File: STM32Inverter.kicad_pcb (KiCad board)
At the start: 4 copper layers, 100 x 100 mm, 151 parts, among them J1 STLINK, J2 CURRENT SENSE, J5 UART, J6 INTERFACE, J7 POWER, J8 501571-2007, J9 RESOLVER, Q1 BCX54, Q2 BCX55, Q4 ST3422A, Q5 BCX54, Q6 BCX55, U1 STM32F303VCTx, U10 ULN2002, U11 LM393, U12 LM393, U2 LM358, U3 AD2S1205, U4 74HCT00, U5 74HCT04, U6 74HCT08, U7 MCP2551-I-SN, U8 74HCT08, U9 74HCT08, Y2 CSTNE8M00GH5C000R0, Y3 CSTNE8M00GH5C000R0

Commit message: Board enven more done
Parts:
- moved C14 1.07 mm to (68.2, 72.8)
- moved C16 0.88 mm to (64.3, 72.8)
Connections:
- U1 pad 73: unconnected-(U1-PF6-Pad73) -> /LED_PIN
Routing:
- net /LED_PIN: track 0.00 -> 18.0 mm, vias 0 -> 2
- net GND: track 81.7 -> 95.6 mm, vias 48 -> 60
- net +5V: track 198.0 -> 211.9 mm, vias 10 -> 11
- net /FAULT_DRV: track 97.2 -> 92.1 mm
- net /VBUS_DRV: track 85.0 -> 81.3 mm
- net /PWM_CH1N: track 78.1 -> 74.4 mm
- net /COS_L: track 52.4 -> 55.5 mm
- net /AD2S1205/Vcc/2: track 15.6 -> 18.5 mm, vias 0 -> 2
- net /ACC_INPUT_A_3V3: track 21.7 -> 24.2 mm
- net /COS_H: track 57.1 -> 59.3 mm
- net Net-(D5-A): track 0.00 -> 2.15 mm
- net Net-(U3-REFBYP): track 2.52 -> 3.29 mm
- net +15V: track 214.7 -> 215.3 mm
- net +5VA: track 127.5 -> 126.9 mm
- net Net-(D2-K): vias 1 -> 2
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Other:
- board text added: "STM32INVERTER MITSUBISHI REMCU Jelcz Industries knowak.xyz"

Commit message: Awaiting review
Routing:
- net +3V3: track 126.2 -> 143.1 mm, vias 17 -> 18
- net +5V: track 211.9 -> 209.0 mm
- net GND: track 95.6 -> 97.6 mm
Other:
- board text added: "1"
- board text added: "DRIVER BOARD"
- board text added: "HALL"
- board text added: "I/O"
- board text added: "MOTOR"
- board text added: "Michał Zychla Krzysztof Nowak"
- board text added: "POWER"
- board text added: "STM32INVERTER MITSUBISHI REMCU Jelcz Industries knowak.xyz 2023"
- board text added: "SWD"
- board text added: "UART"
- board text removed: "STM32INVERTER MITSUBISHI REMCU Jelcz Industries knowak.xyz"

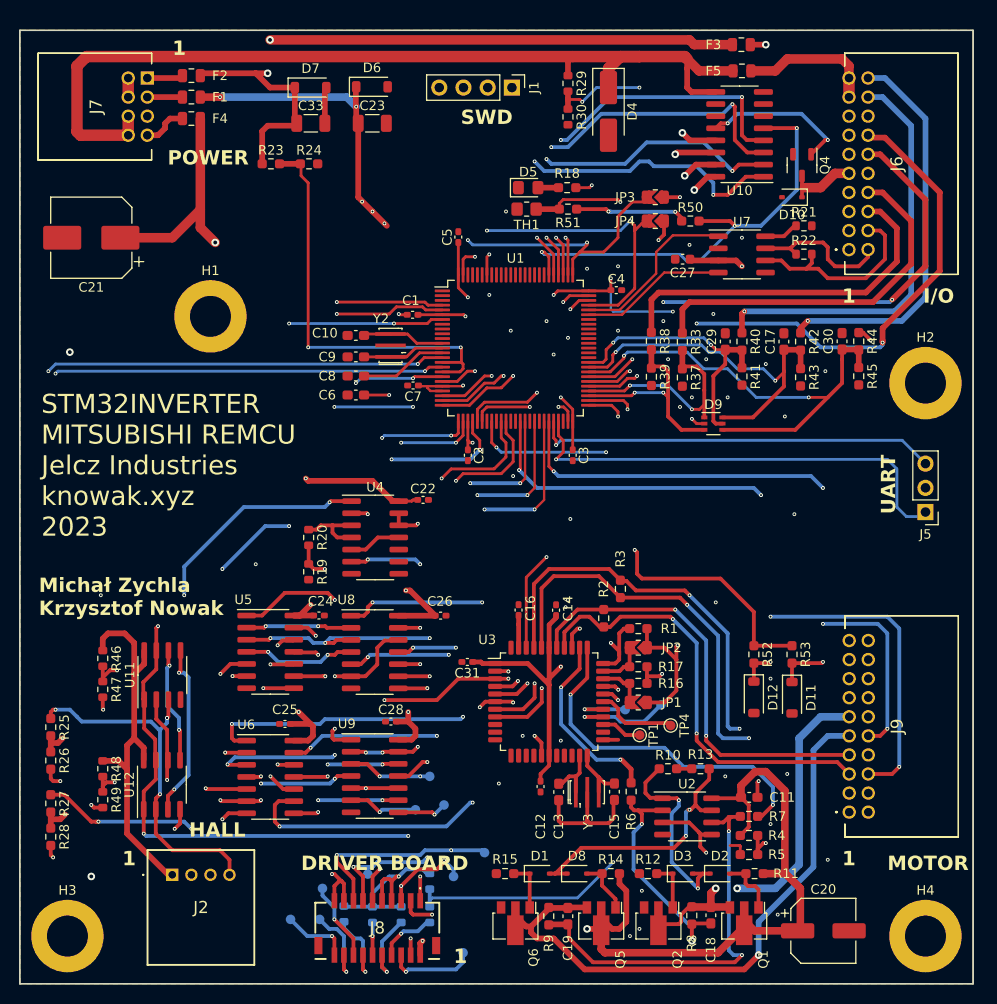
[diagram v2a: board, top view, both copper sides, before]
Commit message: Fix DRC warnings and exclude jumper errors
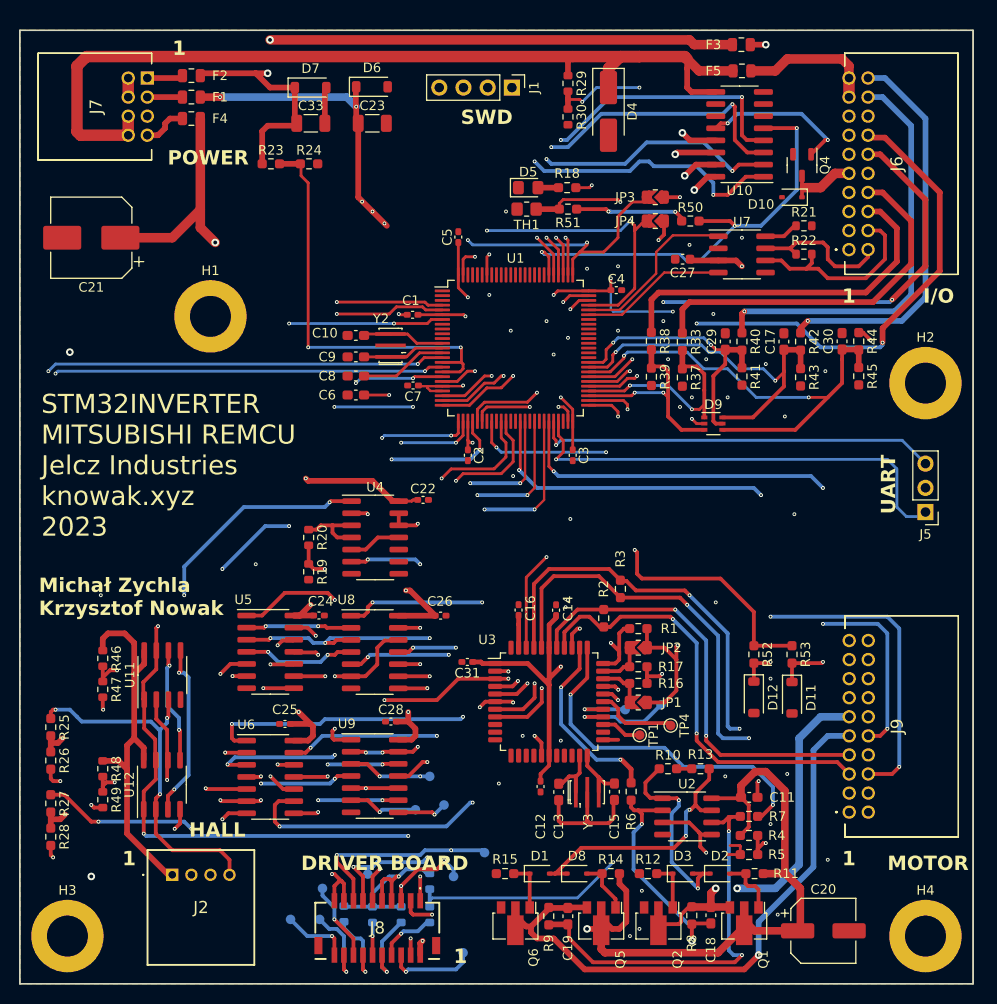
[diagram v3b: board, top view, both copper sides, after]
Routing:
- net GND: track 97.6 -> 99.0 mm
- net /AUX_IN: track 50.3 -> 49.8 mm
- net /CURRENT_B_RAW: vias 4 -> 3
- net /CS_RES: vias 5 -> 4
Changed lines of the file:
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@@
     (property "ki_keywords" "diode")
     (attr smd)
-    (fp_text reference "D10" (at 0 -1.85) (layer "F.SilkS")
+    (fp_text reference "D10" (at 3.25 -0.75) (layer "F.SilkS")
         (effects (font (size 1 1) (thickness 0.15)))
     )
@@
   (segment (start 56.325 41.825) (end 58.575 41.825) (width 0.3) (layer "F.Cu") (net 1))
   (segment (start 89 73) (end 85.5 69.5) (width 0.4) (layer "F.Cu") (net 1))
-  (segment (start 53.925 41.825) (end 53.75 42) (width 0.3) (layer "F.Cu") (net 1))
   (segment (start 49 31) (end 50.5 32.5) (width 0.6) (layer "F.Cu") (net 1))
   (segment (start 47.5 29.5) (end 49 31) (width 0.6) (layer "F.Cu") (net 1))
@@
   (segment (start 47.2875 17.92) (end 47.25 17.9575) (width 0.6) (layer "F.Cu") (net 1))
   (segment (start 58 37.65) (end 58 39) (width 0.3) (layer "F.Cu") (net 1))
-  (segment (start 70.5 30.8375) (end 70.4125 30.75) (width 0.4) (layer "F.Cu") (net 1))
   (segment (start 71.675 39.325) (end 73.925 39.325) (width 0.3) (layer "F.Cu") (net 1))
   (segment (start 59 55) (end 59 53) (width 0.3) (layer "F.Cu") (net 1))
@@
   (segment (start 66.725 88.075) (end 66.725 86.725) (width 0.4) (layer "F.Cu") (net 2))
   (segment (start 69.042894 51.5) (end 68.5 51.5) (width 0.3) (layer "F.Cu") (net 2))
+  (segment (start 87.575 98.45) (end 86.2 98.45) (width 0.3) (layer "F.Cu") (net 2))
   (segment (start 89.5 90.75) (end 89.375 90.875) (width 0.4) (layer "F.Cu") (net 2))
   (segment (start 71.525 91.9125) (end 71.525 94.9125) (width 0.4) (layer "F.Cu") (net 2))
@@
   (segment (start 53.925 45.825) (end 51.5 48.25) (width 0.3) (layer "F.Cu") (net 3))
   (segment (start 51.5 48.25) (end 48.1125 48.25) (width 0.3) (layer "F.Cu") (net 3))
-  (segment (start 48.1125 48.25) (end 48.1375 48.275) (width 0.3) (layer "F.Cu") (net 3))
   (segment (start 56.325 45.825) (end 53.925 45.825) (width 0.3) (layer "F.Cu") (net 3))
   (segment (start 52.575 46.25) (end 53.5 45.325) (width 0.3) (layer "F.Cu") (net 4))
@@
   (segment (start 67.5875 100.45) (end 68.125 100.45) (width 0.4) (layer "F.Cu") (net 16))
   (segment (start 70.875 97.75) (end 68.175 100.45) (width 0.4) (layer "F.Cu") (net 16))
-  (segment (start 82.25 93.75) (end 82.125 93.75) (width 0.4) (layer "F.Cu") (net 16))
   (segment (start 82.375 93.75) (end 82.25 93.75) (width 0.4) (layer "F.Cu") (net 16))
   (segment (start 68.175 100.45) (end 68.125 100.45) (width 0.4) (layer "F.Cu") (net 16))
@@
   (segment (start 99.95 45.475) (end 100 45.525) (width 0.6) (layer "F.Cu") (net 27))
   (segment (start 93.35 53.9) (end 96.75 50.5) (width 0.4) (layer "F.Cu") (net 27))
-  (segment (start 98.25 46.5) (end 98.25 47) (width 0.3) (layer "F.Cu") (net 27))
   (segment (start 100 47.25) (end 100 45.4125) (width 0.6) (layer "F.Cu") (net 27))
   (segment (start 75.375 46.125) (end 75.375 46.375) (width 0.3) (layer "F.Cu") (net 27))
@@
   (segment (start 26.32 77) (end 26.32 79.01) (width 0.4) (layer "F.Cu") (net 42))
   (segment (start 25 96.25) (end 25 93.7) (width 0.4) (layer "F.Cu") (net 42))
-  (segment (start 25 93.7) (end 25 94) (width 0.5) (layer "F.Cu") (net 42))
   (segment (start 44.62 61.38) (end 44.5 61.5) (width 0.4) (layer "F.Cu") (net 42))
   (segment (start 26.205 88.435) (end 26.27 88.5) (width 0.4) (layer "F.Cu") (net 42))
@@
   (segment (start 50 93.75) (end 49.75 94) (width 0.4) (layer "B.Cu") (net 47))
   (segment (start 53.5 93.75) (end 50 93.75) (width 0.4) (layer "B.Cu") (net 47))
-  (segment (start 49 107) (end 49 107.25) (width 0.4) (layer "F.Cu") (net 48))
   (segment (start 58 54.25) (end 57.75 54.5) (width 0.3) (layer "F.Cu") (net 48))
   (segment (start 57.75 54.5) (end 57.25 54.5) (width 0.3) (layer "F.Cu") (net 48))
@@
   (segment (start 100.975 23) (end 101.225 23.25) (width 0.6) (layer "F.Cu") (net 52))
   (segment (start 101.225 23.25) (end 102.75 23.25) (width 0.6) (layer "F.Cu") (net 52))
-  (segment (start 102.5 44.75) (end 102.5 44.5) (width 0.6) (layer "F.Cu") (net 52))
   (segment (start 108.5 37.25) (end 102.5 43.25) (width 0.6) (layer "F.Cu") (net 52))
   (segment (start 81.25 29.5) (end 79.575 29.5) (width 0.4) (layer "F.Cu") (net 52))
@@
   (segment (start 68.775 84.775) (end 72.5 88.5) (width 0.4) (layer "B.Cu") (net 59))
   (segment (start 72.5 88.5) (end 75 88.5) (width 0.4) (layer "B.Cu") (net 59))
-  (segment (start 75 88.5) (end 75.125 88.5) (width 0.4) (layer "B.Cu") (net 59))
   (segment (start 68.775 80.9125) (end 68.775 84.775) (width 0.4) (layer "B.Cu") (net 59))
   (segment (start 69.775 81.6625) (end 71.525 79.9125) (width 0.4) (layer "F.Cu") (net 60))
@@
   (segment (start 63.25 80) (end 63.2375 80.0125) (width 0.4) (layer "F.Cu") (net 84))
   (via (at 60.25 56) (size 0.4) (drill 0.2) (layers "F.Cu" "B.Cu") (net 84))
-  (via (at 60.25 56) (size 0.4) (drill 0.2) (layers "F.Cu" "B.Cu") (net 84))
   (via (at 51 57) (size 0.4) (drill 0.2) (layers "F.Cu" "B.Cu") (net 84))
   (via (at 50.25 82.25) (size 0.4) (drill 0.2) (layers "F.Cu" "B.Cu") (net 84))
@@
   (segment (start 28.705 85.375) (end 28.81 85.48) (width 0.4) (layer "F.Cu") (net 142))
   (segment (start 19.5 95) (end 20.25 95) (width 0.4) (layer "F.Cu") (net 142))
-  (segment (start 20.25 95) (end 20 95) (width 0.4) (layer "F.Cu") (net 142))
   (segment (start 28.81 85.48) (end 28.81 88.5) (width 0.4) (layer "F.Cu") (net 142))
   (segment (start 15.25 92.175) (end 16.675 92.175) (width 0.4) (layer "F.Cu") (net 142))
@@
   (segment (start 37.545 81) (end 37.545 90) (width 0.4) (layer "In1.Cu") (net 151))
   (segment (start 37.545 90) (end 37.295 90.25) (width 0.4) (layer "In1.Cu") (net 151))
-  (segment (start 44.045 79.75) (end 43.795 79.75) (width 0.4) (layer "F.Cu") (net 152))
   (segment (start 44.795 86.25) (end 44.945 86.4) (width 0.4) (layer "F.Cu") (net 152))
   (segment (start 44.795 85.5) (end 44.795 86.25) (width 0.4) (layer "F.Cu") (net 152))
@@
   (segment (start 34 99) (end 33 98) (width 0.4) (layer "F.Cu") (net 160))
   (segment (start 33 98) (end 28 98) (width 0.4) (layer "F.Cu") (net 160))
-  (via (at 27.455 84.125) (size 0.4) (drill 0.2) (layers "F.Cu" "B.Cu") (net 160))
   (via (at 15.75 83.25) (size 0.4) (drill 0.2) (layers "F.Cu" "B.Cu") (net 160))
   (via (at 27.455 84.125) (size 0.4) (drill 0.2) (layers "F.Cu" "B.Cu") (net 160))
@@
   (segment (start 86.5 32) (end 87 32.5) (width 0.4) (layer "F.Cu") (net 173))
   (segment (start 67.5 35.75) (end 67 35.25) (width 0.3) (layer "F.Cu") (net 173))
-  (segment (start 93.3375 22.25) (end 93.5 22.25) (width 0.4) (layer "F.Cu") (net 173))
   (segment (start 67.5 37.65) (end 67.5 35.75) (width 0.3) (layer "F.Cu") (net 173))
   (segment (start 86.5 32) (end 83.25 32) (width 0.4) (layer "F.Cu") (net 173))

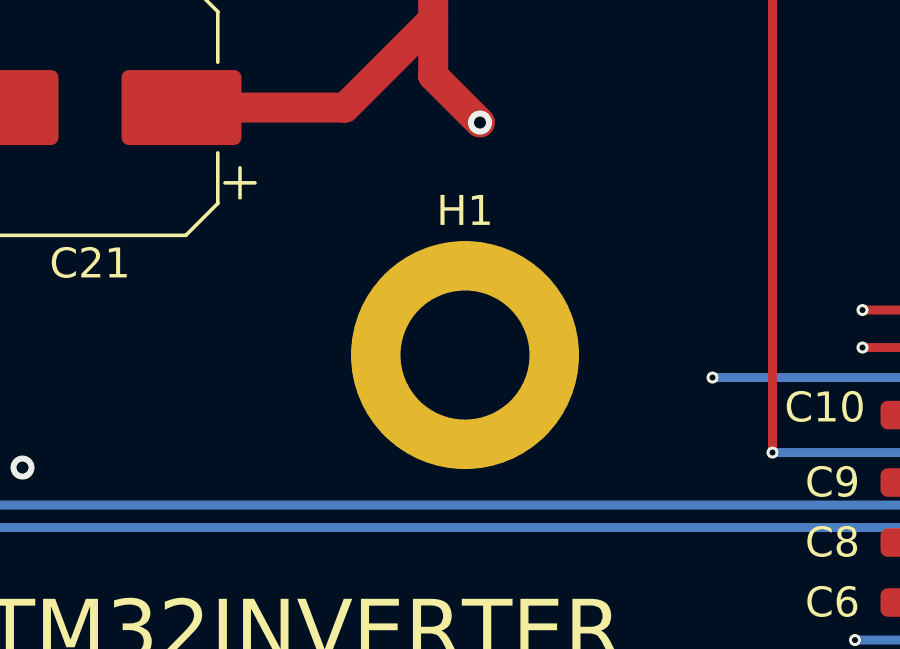
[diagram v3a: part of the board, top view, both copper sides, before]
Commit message: Hole moved
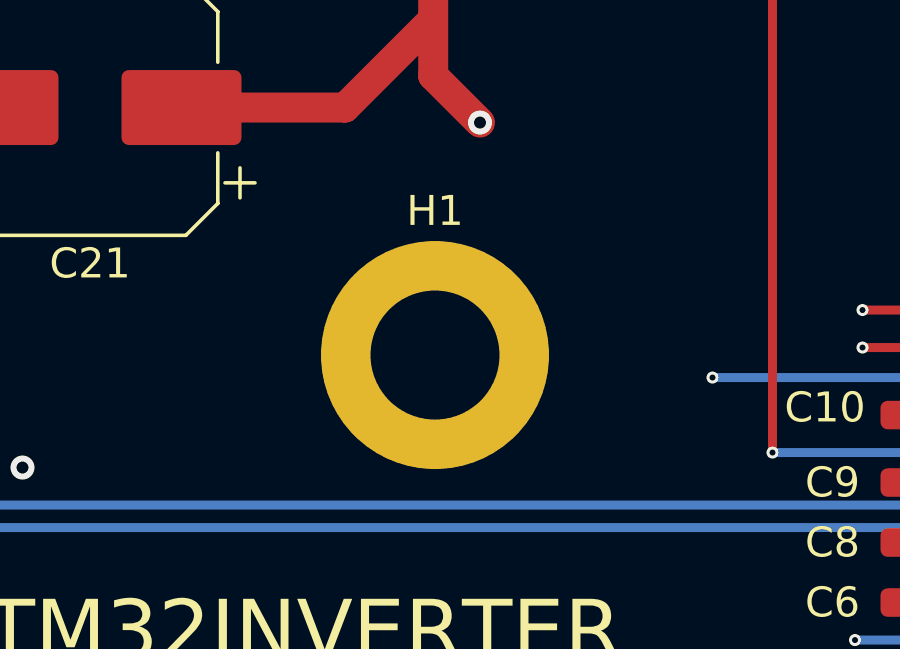
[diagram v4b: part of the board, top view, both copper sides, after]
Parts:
- moved H1 1.00 mm to (31.0, 42.0)
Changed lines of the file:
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@@
   )
   (footprint "MountingHole:MountingHole_4.3mm_M4_ISO7380_Pad" (layer "F.Cu")
-    (at 32 42)
+    (at 31 42)
     (descr "Mounting Hole 4.3mm, M4, ISO7380")
     (tags "mounting hole 4.3mm m4 iso7380")

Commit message: Review done
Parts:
- added JP5: ~, MEMS_Passive:R_0805_2012Metric_Jumper, B.Cu at (87.7, 39.2)
- added JP6: ~, MEMS_Passive:R_0805_2012Metric_Jumper, B.Cu at (92.6, 39.2)
- moved C21 1.27 mm to (19.3, 35.0)
- moved D10 1.00 mm to (94.0, 29.5)
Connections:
- U4 pad 10: (no net) -> GND
- U4 pad 8: (no net) -> unconnected-(U4-Pad8)
- U4 pad 9: (no net) -> GND
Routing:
- net +3V3: track 142.7 -> 130.8 mm, vias 18 -> 16
- net GND: track 99.0 -> 110.1 mm, vias 60 -> 108
- net Net-(J6-Pad14): track 66.0 -> 72.4 mm, vias 3 -> 4
- net +5VA: track 126.9 -> 131.6 mm
- net /ACC_INPUT_A_3V3: track 24.2 -> 21.8 mm
- net /CS_RES: track 52.5 -> 51.1 mm, vias 4 -> 3
- net Net-(J6-Pad12): track 53.0 -> 54.2 mm, vias 3 -> 2
- net Net-(J6-Pad1): track 12.0 -> 11.0 mm
- net /KEY_IN: track 39.2 -> 40.1 mm
- net /MAIN_OUT_OD: track 7.52 -> 8.28 mm
- net /V_HIGH: vias 3 -> 2
- net /RDVEL: vias 3 -> 2
- net /2.5V: vias 2 -> 3
- added copper zone on B.Cu, net GND
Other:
- board text added: "3.3V"
- board text added: "GND"
- board text added: "INVERTER32 MITSUBISHI REMCU Michał Zychla Krzysztof Nowak 2023"
- board text added: "RX"
- board text added: "SWCLK"
- board text added: "SWDIO"
- board text added: "TX"
- board text added: "https://github.com/Zychlix/Inverter32"
- board text removed: "Michał Zychla Krzysztof Nowak"
- board text removed: "STM32INVERTER MITSUBISHI REMCU Jelcz Industries knowak.xyz 2023"
